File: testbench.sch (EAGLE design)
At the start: 40 parts, among them T1 C8492, T2 C8492, T3 C8545, T4 C8545, X1 MKDSN1,5/2-5,08

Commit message: routing and placement updated, dimensions changed
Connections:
- removed net N$18: JP1.TOTAL-C, R12.1
- net GND: now also JP1.TOTAL-C, R12.1
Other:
- moved on the sheet: D1, D2, R21, R22, R23, R24, R25, R26, T3, T4, U$1, X1-1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

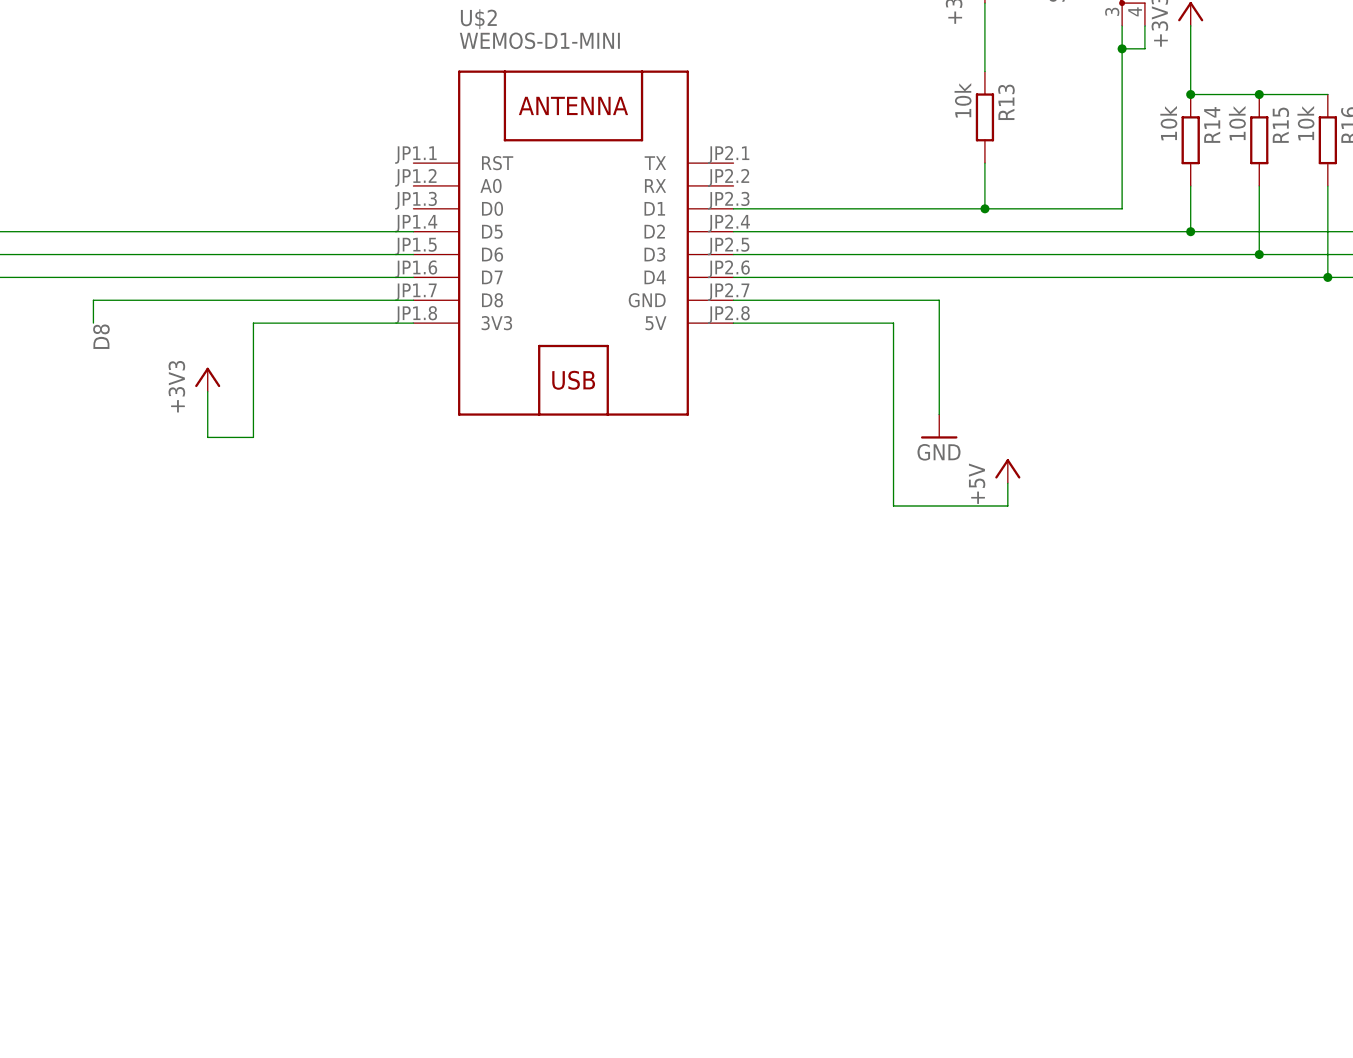
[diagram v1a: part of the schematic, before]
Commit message: display added
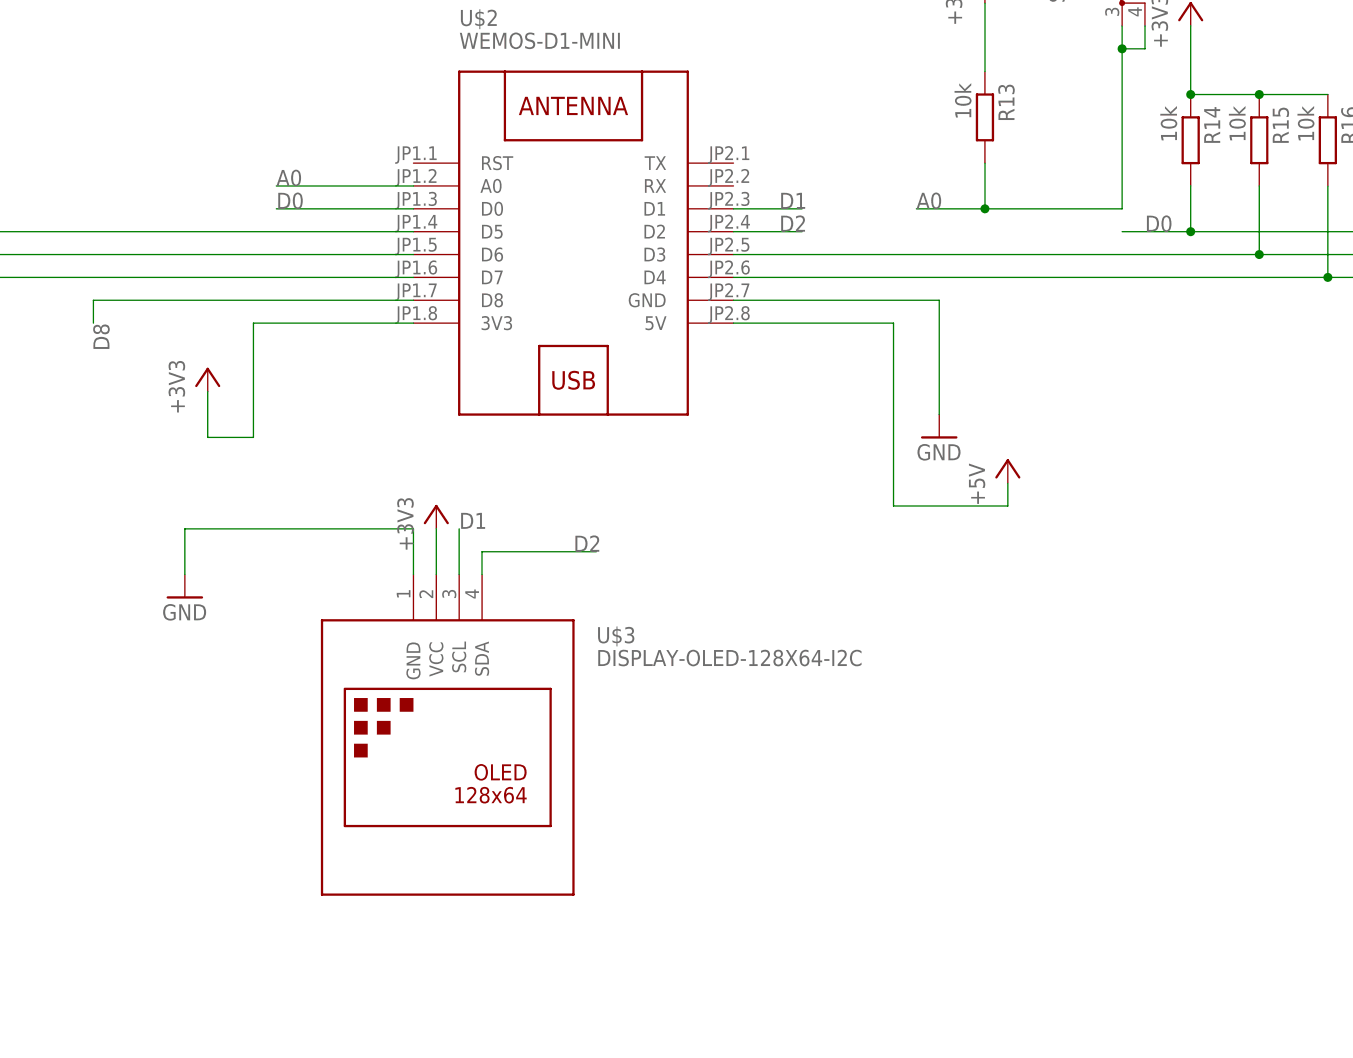
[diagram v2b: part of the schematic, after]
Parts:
- added U$3: DISPLAY-OLED-128X64-I2C, diy-modules:DISPLAY-OLED-128X64-I2C
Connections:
- removed net N$12: R13.2, S1.P, S1.P1, U$2.D1
- removed net N$13: R14.2, SW1.1, U$2.D2
- new net A0: R13.2, S1.P, S1.P1, U$2.A0
- new net D0: R14.2, SW1.1, U$2.D0
- new net D1: U$2.D1, U$3.SCL
- new net D2: U$2.D2, U$3.SDA
- net +3V3: now also U$3.VCC
- net GND: now also U$3.GND

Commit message: routing updated
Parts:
- added H1, H2, H3, H4: MOUNT-PAD-ROUND3.2, holes:MOUNT-PAD-ROUND3.2
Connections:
- net GND: now also H1.MOUNT, H2.MOUNT, H3.MOUNT, H4.MOUNT
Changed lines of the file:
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@@
 <part name="GND10" library="supply1" library_urn="urn:adsk.eagle:library:371" deviceset="GND" device=""/>
 <part name="+3V4" library="supply1" library_urn="urn:adsk.eagle:library:371" deviceset="+3V3" device=""/>
+<part name="H1" library="holes" library_urn="urn:adsk.eagle:library:237" deviceset="MOUNT-PAD-ROUND" device="3.2" package3d_urn="urn:adsk.eagle:package:14282/1"/>
+<part name="H2" library="holes" library_urn="urn:adsk.eagle:library:237" deviceset="MOUNT-PAD-ROUND" device="3.2" package3d_urn="urn:adsk.eagle:package:14282/1"/>
+<part name="H3" library="holes" library_urn="urn:adsk.eagle:library:237" deviceset="MOUNT-PAD-ROUND" device="3.2" package3d_urn="urn:adsk.eagle:package:14282/1"/>
+<part name="H4" library="holes" library_urn="urn:adsk.eagle:library:237" deviceset="MOUNT-PAD-ROUND" device="3.2" package3d_urn="urn:adsk.eagle:package:14282/1"/>
+<part name="GND11" library="supply1" library_urn="urn:adsk.eagle:library:371" deviceset="GND" device=""/>
 </parts>
 <sheets>
@@
 <instance part="+3V4" gate="G$1" x="215.9" y="91.44" smashed="yes">
 <attribute name="VALUE" x="213.36" y="86.36" size="1.778" layer="96" rot="R90"/>
+</instance>
+<instance part="H1" gate="G$1" x="259.08" y="208.28" smashed="yes">
+<attribute name="NAME" x="261.874" y="208.8642" size="1.778" layer="95"/>
+<attribute name="VALUE" x="261.874" y="205.8162" size="1.778" layer="96"/>
+</instance>
+<instance part="H2" gate="G$1" x="259.08" y="198.12" smashed="yes">
+<attribute name="NAME" x="261.874" y="198.7042" size="1.778" layer="95"/>
+<attribute name="VALUE" x="261.874" y="195.6562" size="1.778" layer="96"/>
+</instance>
+<instance part="H3" gate="G$1" x="259.08" y="187.96" smashed="yes">
+<attribute name="NAME" x="261.874" y="188.5442" size="1.778" layer="95"/>
+<attribute name="VALUE" x="261.874" y="185.4962" size="1.778" layer="96"/>
+</instance>
+<instance part="H4" gate="G$1" x="259.08" y="177.8" smashed="yes">
+<attribute name="NAME" x="261.874" y="178.3842" size="1.778" layer="95"/>
+<attribute name="VALUE" x="261.874" y="175.3362" size="1.778" layer="96"/>
+</instance>
+<instance part="GND11" gate="1" x="251.46" y="167.64" smashed="yes">
+<attribute name="VALUE" x="248.92" y="165.1" size="1.778" layer="96"/>
 </instance>
 </instances>
@@
 <pinref part="GND10" gate="1" pin="GND"/>
 </segment>
-</net>
+<segment>
+<pinref part="H4" gate="G$1" pin="MOUNT"/>
+<pinref part="GND11" gate="1" pin="GND"/>
+<wire x1="256.54" y1="177.8" x2="251.46" y2="177.8" width="0.1524" layer="91"/>
+<wire x1="251.46" y1="177.8" x2="251.46" y2="170.18" width="0.1524" layer="91"/>
+<pinref part="H3" gate="G$1" pin="MOUNT"/>
+<wire x1="256.54" y1="187.96" x2="251.46" y2="187.96" width="0.1524" layer="91"/>
+<wire x1="251.46" y1="187.96" x2="251.46" y2="177.8" width="0.1524" layer="91"/>
+<junction x="251.46" y="177.8"/>
+<pinref part="H2" gate="G$1" pin="MOUNT"/>
+<wire x1="256.54" y1="198.12" x2="251.46" y2="198.12" width="0.1524" layer="91"/>
+<wire x1="251.46" y1="198.12" x2="251.46" y2="187.96" width="0.1524" layer="91"/>
+<junction x="251.46" y="187.96"/>
+<pinref part="H1" gate="G$1" pin="MOUNT"/>
+<wire x1="256.54" y1="208.28" x2="251.46" y2="208.28" width="0.1524" layer="91"/>
+<wire x1="251.46" y1="208.28" x2="251.46" y2="198.12" width="0.1524" layer="91"/>
+<junction x="251.46" y="198.12"/>
+</segment>
+</net>

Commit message: text added and diodes defined
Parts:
- added R27, R28: 2k2, rcl:R-EU_R0805
- D1, D2: value (none) -> C8062
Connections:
- net +3V3: now also R27.1, R28.1
- net D1: now also R28.2
- net D2: now also R27.2
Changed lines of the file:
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@@
 <part name="R21" library="rcl" library_urn="urn:adsk.eagle:library:334" deviceset="R-EU_" device="R0805" package3d_urn="urn:adsk.eagle:package:23553/2" value="10k"/>
 <part name="R22" library="rcl" library_urn="urn:adsk.eagle:library:334" deviceset="R-EU_" device="R0805" package3d_urn="urn:adsk.eagle:package:23553/2" value="10k"/>
-<part name="D1" library="semicon-smd-ipc" library_urn="urn:adsk.eagle:library:353" deviceset="D-FILL-" device="MLL-34" package3d_urn="urn:adsk.eagle:package:26305/1"/>
+<part name="D1" library="semicon-smd-ipc" library_urn="urn:adsk.eagle:library:353" deviceset="D-FILL-" device="MLL-34" package3d_urn="urn:adsk.eagle:package:26305/1" value="C8062"/>
 <part name="R23" library="rcl" library_urn="urn:adsk.eagle:library:334" deviceset="R-EU_" device="R0805" package3d_urn="urn:adsk.eagle:package:23553/2" value="10k"/>
 <part name="P+5" library="supply1" library_urn="urn:adsk.eagle:library:371" deviceset="VCC" device=""/>
@@
 <part name="R24" library="rcl" library_urn="urn:adsk.eagle:library:334" deviceset="R-EU_" device="R0805" package3d_urn="urn:adsk.eagle:package:23553/2" value="10k"/>
 <part name="R25" library="rcl" library_urn="urn:adsk.eagle:library:334" deviceset="R-EU_" device="R0805" package3d_urn="urn:adsk.eagle:package:23553/2" value="10k"/>
-<part name="D2" library="semicon-smd-ipc" library_urn="urn:adsk.eagle:library:353" deviceset="D-FILL-" device="MLL-34" package3d_urn="urn:adsk.eagle:package:26305/1"/>
+<part name="D2" library="semicon-smd-ipc" library_urn="urn:adsk.eagle:library:353" deviceset="D-FILL-" device="MLL-34" package3d_urn="urn:adsk.eagle:package:26305/1" value="C8062"/>
 <part name="R26" library="rcl" library_urn="urn:adsk.eagle:library:334" deviceset="R-EU_" device="R0805" package3d_urn="urn:adsk.eagle:package:23553/2" value="10k"/>
 <part name="P+6" library="supply1" library_urn="urn:adsk.eagle:library:371" deviceset="VCC" device=""/>
@@
 <part name="H4" library="holes" library_urn="urn:adsk.eagle:library:237" deviceset="MOUNT-PAD-ROUND" device="3.2" package3d_urn="urn:adsk.eagle:package:14282/1"/>
 <part name="GND11" library="supply1" library_urn="urn:adsk.eagle:library:371" deviceset="GND" device=""/>
+<part name="R27" library="rcl" library_urn="urn:adsk.eagle:library:334" deviceset="R-EU_" device="R0805" package3d_urn="urn:adsk.eagle:package:23553/2" value="2k2"/>
+<part name="R28" library="rcl" library_urn="urn:adsk.eagle:library:334" deviceset="R-EU_" device="R0805" package3d_urn="urn:adsk.eagle:package:23553/2" value="2k2"/>
 </parts>
 <sheets>
@@
 <attribute name="VALUE" x="185.42" y="78.74" size="1.778" layer="96"/>
 </instance>
-<instance part="+3V4" gate="G$1" x="215.9" y="91.44" smashed="yes">
-<attribute name="VALUE" x="213.36" y="86.36" size="1.778" layer="96" rot="R90"/>
+<instance part="+3V4" gate="G$1" x="215.9" y="106.68" smashed="yes">
+<attribute name="VALUE" x="213.36" y="101.6" size="1.778" layer="96" rot="R90"/>
 </instance>
 <instance part="H1" gate="G$1" x="259.08" y="208.28" smashed="yes">
@@
 <instance part="GND11" gate="1" x="251.46" y="167.64" smashed="yes">
 <attribute name="VALUE" x="248.92" y="165.1" size="1.778" layer="96"/>
+</instance>
+<instance part="R27" gate="G$1" x="226.06" y="96.52" smashed="yes">
+<attribute name="NAME" x="222.25" y="98.0186" size="1.778" layer="95"/>
+<attribute name="VALUE" x="222.25" y="93.218" size="1.778" layer="96"/>
+</instance>
+<instance part="R28" gate="G$1" x="226.06" y="91.44" smashed="yes">
+<attribute name="NAME" x="222.25" y="92.9386" size="1.778" layer="95"/>
+<attribute name="VALUE" x="222.25" y="88.138" size="1.778" layer="96"/>
 </instance>
 </instances>
@@
 <segment>
 <pinref part="U$3" gate="G$1" pin="VCC"/>
-<wire x1="215.9" y1="83.82" x2="215.9" y2="88.9" width="0.1524" layer="91"/>
+<wire x1="215.9" y1="83.82" x2="215.9" y2="91.44" width="0.1524" layer="91"/>
 <pinref part="+3V4" gate="G$1" pin="+3V3"/>
+<pinref part="R27" gate="G$1" pin="1"/>
+<wire x1="215.9" y1="91.44" x2="215.9" y2="96.52" width="0.1524" layer="91"/>
+<wire x1="215.9" y1="96.52" x2="215.9" y2="104.14" width="0.1524" layer="91"/>
+<wire x1="220.98" y1="96.52" x2="215.9" y2="96.52" width="0.1524" layer="91"/>
+<junction x="215.9" y="96.52"/>
+<pinref part="R28" gate="G$1" pin="1"/>
+<wire x1="220.98" y1="91.44" x2="215.9" y2="91.44" width="0.1524" layer="91"/>
+<junction x="215.9" y="91.44"/>
 </segment>
 </net>
@@
 <wire x1="218.44" y1="83.82" x2="218.44" y2="88.9" width="0.1524" layer="91"/>
 <label x="218.44" y="88.9" size="1.778" layer="95"/>
+<wire x1="218.44" y1="88.9" x2="231.14" y2="88.9" width="0.1524" layer="91"/>
+<pinref part="R28" gate="G$1" pin="2"/>
+<wire x1="231.14" y1="88.9" x2="231.14" y2="91.44" width="0.1524" layer="91"/>
 </segment>
 </net>
@@
 <wire x1="220.98" y1="86.36" x2="233.68" y2="86.36" width="0.1524" layer="91"/>
 <label x="231.14" y="86.36" size="1.778" layer="95"/>
-</segment>
-</net>
+<pinref part="R27" gate="G$1" pin="2"/>
+<wire x1="231.14" y1="96.52" x2="233.68" y2="96.52" width="0.1524" layer="91"/>
+<wire x1="233.68" y1="96.52" x2="233.68" y2="86.36" width="0.1524" layer="91"/>
+</segment>
+</net>
